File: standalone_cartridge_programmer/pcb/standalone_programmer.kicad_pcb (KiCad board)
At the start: 2 copper layers, 70 x 65 mm, 11 parts, among them CON1 cartridge port, CON2 AVR ISP, CON3 jtag, U1 Pro Micro 5V, U2 XC9572XL, U3 MCP1700T-3302E/MB

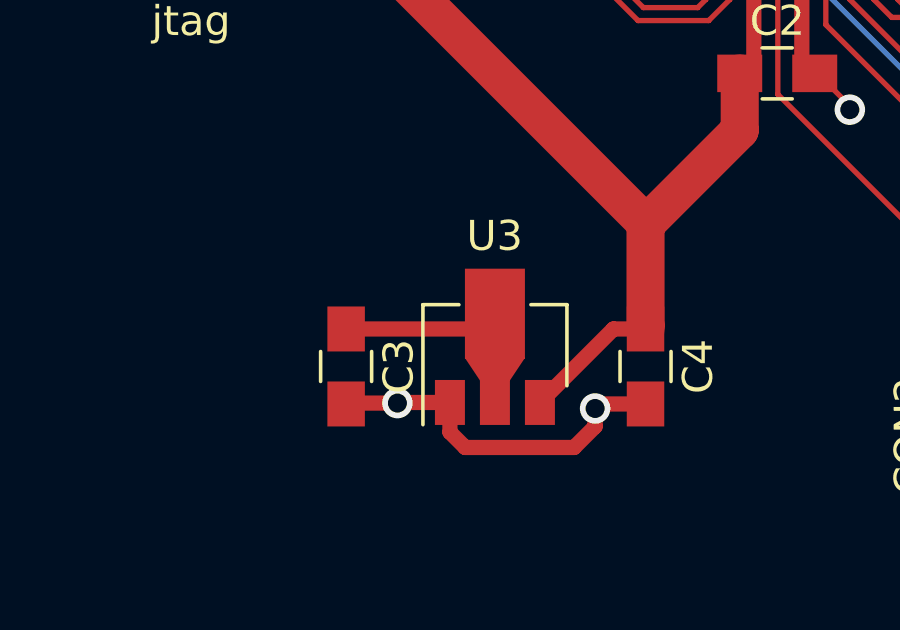
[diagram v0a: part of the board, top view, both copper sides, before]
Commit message: standalone_cartridge_programmer: Added latest code, switched to new gerber build script
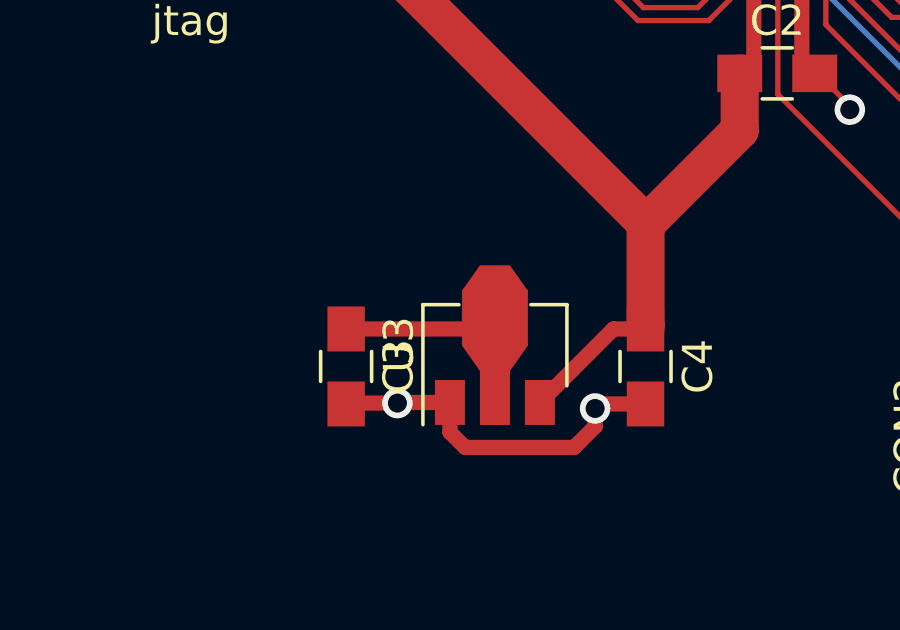
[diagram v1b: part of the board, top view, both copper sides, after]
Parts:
- U3: footprint TO_SOT_Packages_SMD:SOT89-3_Housing -> TO_SOT_Packages_SMD:SOT-89-3

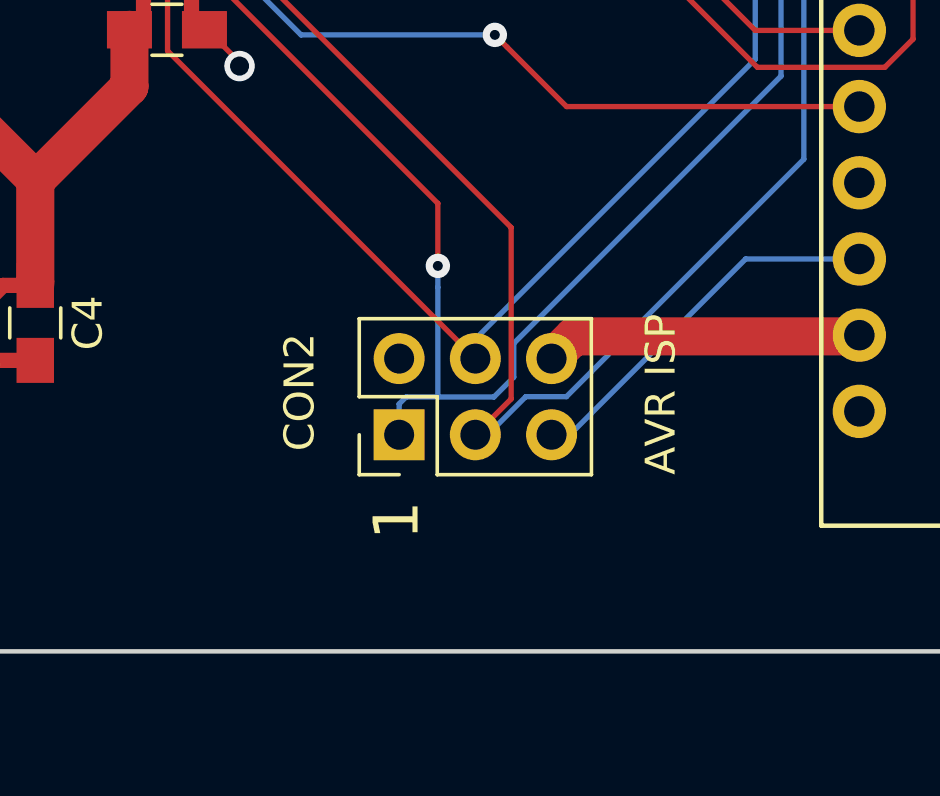
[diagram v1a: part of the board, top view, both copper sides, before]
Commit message: Silkscreen and BOM updates
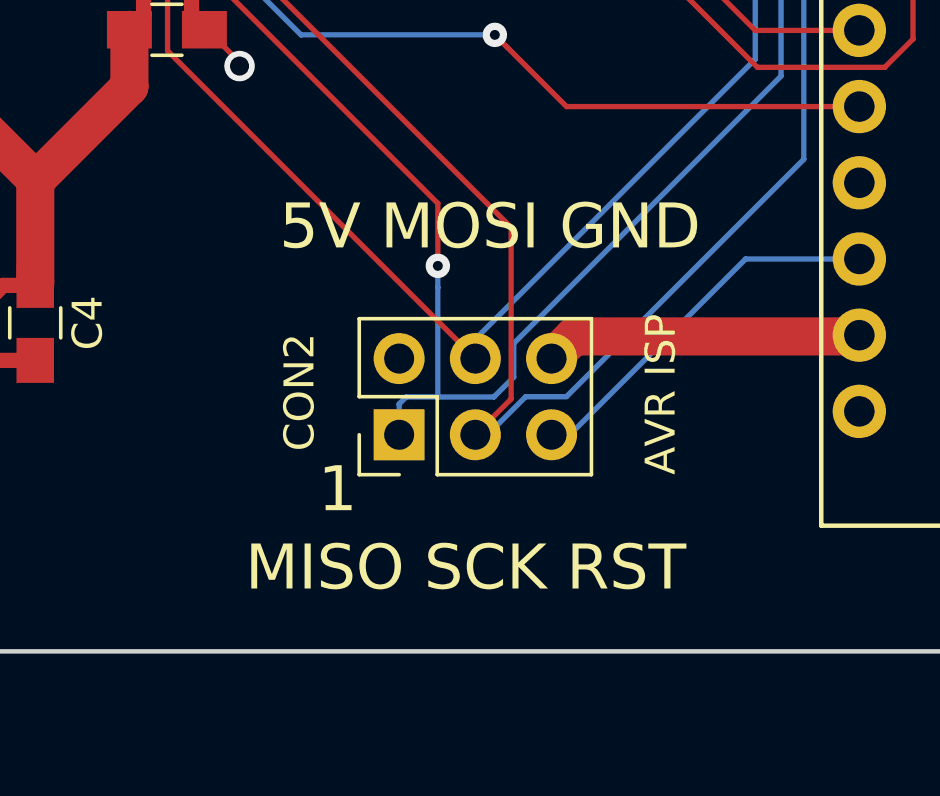
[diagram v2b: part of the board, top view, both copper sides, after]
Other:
- board text added: "5V MOSI GND"
- board text added: "MISO SCK RST"
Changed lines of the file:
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@@
-(kicad_pcb (version 4) (host pcbnew 4.0.6)
+(kicad_pcb (version 20171130) (host pcbnew "(5.0.1-3-g963ef8bb5)")
   (general
-    (links 82)
-    (no_connects 0)
-    (area 129.924999 49.924999 200.075001 115.075001)
     (thickness 1.6)
-    (drawings 14)
+    (drawings 16)
     (tracks 384)
     (zones 0)
@@
     (pad_drill 0.762)
     (pad_to_mask_clearance 0.2)
+    (solder_mask_min_width 0.25)
     (aux_axis_origin 0 0)
     (visible_elements FFFFFF7F)
@@
       (layerselection 0x010fc_80000001)
       (usegerberextensions true)
+      (usegerberattributes false)
+      (usegerberadvancedattributes false)
+      (creategerberjobfile false)
       (excludeedgelayer true)
       (linewidth 0.100000)
@@
       (hpglpennumber 1)
       (hpglpenspeed 20)
-      (hpglpendiameter 15)
-      (hpglpenoverlay 2)
+      (hpglpendiameter 15.000000)
       (psnegative false)
       (psa4output false)
@@
       (drillshape 0)
       (scaleselection 1)
-      (outputdirectory gerbers/))
+      (outputdirectory "gerbers/"))
   )
   (net 0 "")
@@
       (net 2 GND))
     (model ${KISYS3DMOD}/Pin_Headers.3dshapes/Pin_Header_Straight_2x03_Pitch2.54mm.wrl
-      (at (xyz 0.05 -0.1 0))
+      (offset (xyz 1.269999980926514 -2.539999961853027 0))
       (scale (xyz 1 1 1))
       (rotate (xyz 0 0 90))
@@
       (net 2 GND))
     (model ${KISYS3DMOD}/Pin_Headers.3dshapes/Pin_Header_Straight_2x05_Pitch2.54mm.wrl
-      (at (xyz 0.05 -0.2 0))
+      (offset (xyz 1.269999980926514 -5.079999923706055 0))
       (scale (xyz 1 1 1))
       (rotate (xyz 0 0 90))
@@
     )
   )
+  (gr_text "5V MOSI GND" (at 166.96 100.84) (layer F.SilkS)
+    (effects (font (size 1.5 1.5) (thickness 0.3)))
+  )
+  (gr_text "MISO SCK RST" (at 166.15 112.21) (layer F.SilkS)
+    (effects (font (size 1.5 1.5) (thickness 0.3)))
+  )
   (gr_text "Acorn Electron Cartridge USB Interface rev 2\nPhillip Pearson <pp@myelin.nz>\nCopyright 2017 Google Inc" (at 165 69) (layer B.SilkS)
     (effects (font (size 1.5 1.5) (thickness 0.3)) (justify mirror))
   )
-  (gr_text 1 (at 163.85 110.63 90) (layer F.SilkS)
+  (gr_text 1 (at 161.88 109.6) (layer F.SilkS)
     (effects (font (size 1.5 1.5) (thickness 0.3)))
   )
